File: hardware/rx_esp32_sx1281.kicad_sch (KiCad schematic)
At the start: 0 parts

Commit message: wip: schematic sheets in progress
Co-Authored-By: Claude Opus 5.5 <noreply@anthropic.com>
Claude-Session: https://claude.ai/code/session_01RFaS5jnC9tnPam9GBgmGnG
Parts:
- added AE1: ANT 2.4G wire, lib:AE_WireHole_PTH0.5mm, symbol Device:Antenna
- added AE2: 2450AT07A0100001T, lib:ANT-SMD_4P-L1.0-W0.5_Johanson_2450AT07A0100_Edge5.0x3.2, symbol lib:2450AT07A0100001T
- added C132, C133: 1.2pF, lib:C_0201_0603Metric_W, symbol Device:C
- added C73, C92: 1uF, lib:C_0201_0603Metric_W, symbol Device:C
- added C76, C83, C85, C89, C91: 100nF, lib:C_0201_0603Metric_W, symbol Device:C
- added C82: 10uF, lib:C_0402_1005Metric_W, symbol Device:C
- added C84: 1nF, lib:C_0201_0603Metric_W, symbol Device:C
- added C86, C88: 10nF, lib:C_0201_0603Metric_W, symbol Device:C
- added C87: 470nF, lib:C_0201_0603Metric_W, symbol Device:C
- added D4: RGB WS2812, lib:LED-SMD_4P-L1.0-W1.0-TL_XL-1010RGBC-WS2812B_Dense, symbol OpenDrone:XL-1010RGBC-WS2812B
- added D8: SDM02M30CLP3, lib:X2-DFN1006-3_L1.0-W0.6_SDM02M30CLP3, symbol lib:SDM02M30CLP3-7B
- added FL1: LPF 2.4G, lib:FILTER-SMD_4P-L1.0-W0.5-L_DEA102700LT-XXX_W, symbol OpenDrone:DEA102700LT-6307A2
- added R56: 10k, lib:R_0201_0603Metric_W, symbol Device:R
- added R88: 0R, lib:R_0201_0603Metric_W, symbol Device:R
- added SW1: SKUBAAE010, lib:SW_Alps_SKUBAAE010_2.4x1.4mm, symbol lib:SKUBAAE010
- added U16: ESP32-PICO-V3, lib:LGA-48_7x7mm_P0.5mm_EP_ESP32-PICO, symbol lib:ESP32-PICO-V3
- added U18: SX1281, lib:QFN-24_L4.0-W4.0-P0.50-TL-EP2.6_Dense, symbol lib:SX1281IMLTRT
- added X3: 52MHz TCXO, lib:OSC-SMD_4P-L2.0-W1.6-BL_TXC_7Z_Dense, symbol OpenDrone:OW7EL89CENUNFAYLC-52M
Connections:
- new net +3V3: C76.1, C82.1, C83.1, C85.1, C89.1, C91.1, C92.1, D4.2 (VDD), R56.1, U16.1 (VDDA), U16.19 (VDD3P3_RTC), U16.3 (VDDA3P3), U16.37 (VDD3P3_CPU), U16.4 (VDDA3P3), U16.43 (VDDA), U16.46 (VDDA), U18.11 (VBAT_IO), U18.15 (VBAT), X3.4 (VDD)
- new net BOOT_SW: D8.3 (K), SW1.1
- new net FC_BOOT: D8.1 (A1)
- new net GND: AE2.2 (GND), AE2.3 (GND), C132.2, C133.2, C73.2, C76.2, C82.2, C83.2, C85.2, C86.2, C87.1, C88.1, C89.2, C91.2, C92.2, D4.3 (GND), FL1.2 (GND), FL1.4 (GND), SW1.2, U16.49 (GND), U18.13 (GND), U18.20 (GND), U18.21 (GND), U18.23 (GND), U18.24 (GND), U18.25 (GND), U18.5 (GND), X3.1 (GND), X3.2 (GND)
- new net PA_BIAS_PWM: U16.20 (MTCK/IO13)
- new net PA_DET: U16.24 (IO4)
- new net PA_EN: U16.22 (IO2)
- new net PA_NTC: U16.10 (VDET_1/I34)
- new net RADIO_BUSY: U16.5 (SENSOR_VP/I36), U18.7 (BUSY)
- new net RADIO_DIO1: U16.6 (SENSOR_CAPP/I37), U18.8 (DIO1)
- new net RADIO_MISO: U16.13 (32K_XN/IO33), U18.16 (MISO_TX)
- new net RADIO_MOSI: U16.12 (32K_XP/IO32), U18.17 (MOSI_RX)
- new net RADIO_NSS: U16.16 (IO27), U18.19 (NSS_CTS)
- new net RADIO_RST: U16.15 (IO26), U18.3 (NRESET)
- new net RADIO_SCK: U16.14 (IO25), U18.18 (SCK_RTSN)
- new net RF_RFIO: FL1.1 (IN), U18.22 (RFIO)
- new net RF_RX_ANT: AE1.1 (A), FL1.3 (OUT)
- new net RF_WIFI: C133.1, R88.2, U16.2 (LNA_IN)
- new net RF_WIFI_ANT: AE2.1 (FEED), AE2.4 (FEED), C132.1, R88.1
- new net RX_BOOT: D8.2 (A2), U16.23 (IO0)
- new net RX_EN: C73.1, R56.2, U16.9 (EN)
- new net RX_LED: D4.4 (DIN), U16.39 (IO22)
- new net TCXO_OUT: C84.1, X3.3 (Out_Put)
- new net UART0_RX: U16.41 (U0TXD/IO1)
- new net UART0_TX: U16.40 (U0RXD/IO3)
- new net VREG_RADIO: C87.2, C88.2, U18.12 (DCC_FB), U18.2 (VDD_IN)
- new net VR_PA: C86.1, U18.1 (VR_PA)
- new net VTX_PWR_CTL: U16.42 (IO21)
- new net VTX_SPI_CLK: U16.34 (IO5)
- new net VTX_SPI_CS: U16.38 (IO19)
- new net VTX_SPI_DATA: U16.17 (MTMS/IO14)
- new net XTA: C84.2, U18.4 (XTA)
- no-connect marks 0 -> 25
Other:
- note added: "2.4 GHz LPF + wire antenna"
- note added: "Boot / bind button"
- note added: "ELRS RGB LED"
- note added: "ESP32-PICO-V3 MCU"
- note added: "SX1281 radio"
- note added: "Wi-Fi chip antenna"

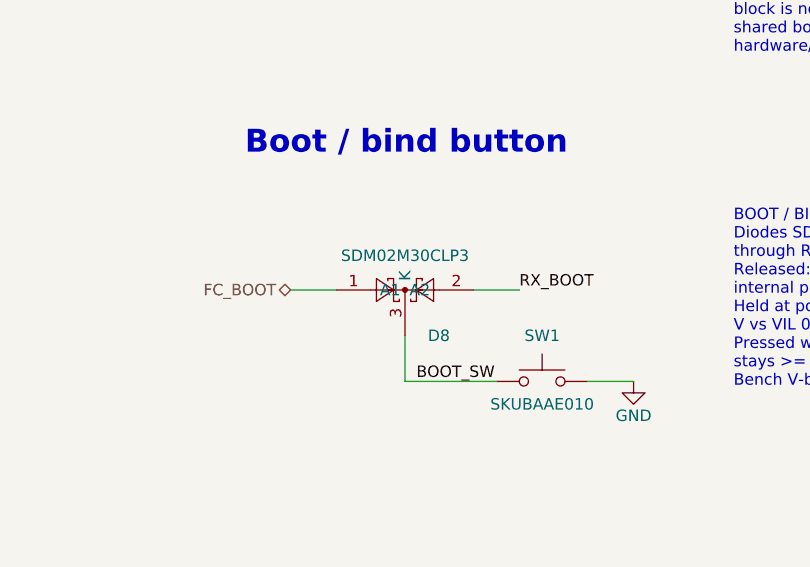
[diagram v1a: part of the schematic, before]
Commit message: wip: schematic integration in progress (saved after container restart)
Co-Authored-By: Claude Opus 5.5 <noreply@anthropic.com>
Claude-Session: https://claude.ai/code/session_01RFaS5jnC9tnPam9GBgmGnG
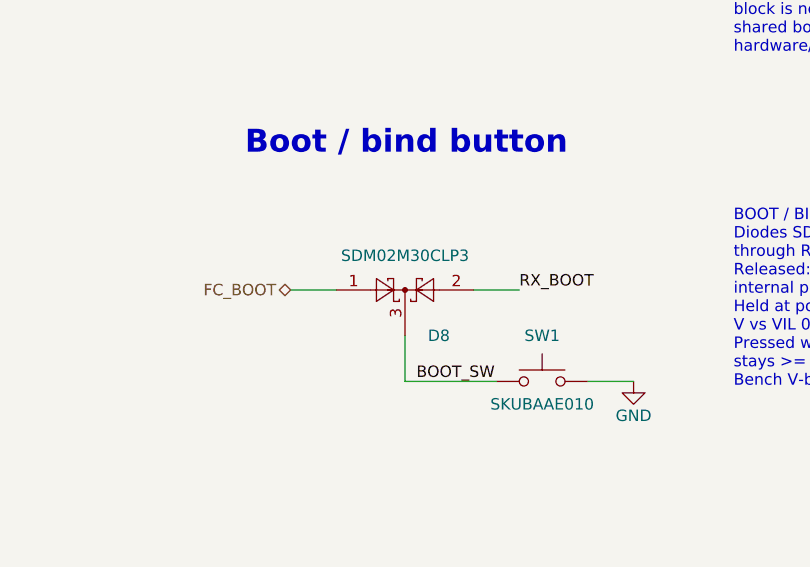
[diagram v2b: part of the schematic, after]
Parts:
- C82: LCSC (none) -> C237279
- D4: symbol OpenDrone:XL-1010RGBC-WS2812B -> lib:XL-1010RGBC-WS2812B
- FL1: symbol OpenDrone:DEA102700LT-6307A2 -> lib:DEA102700LT-6307A2
- X3: symbol OpenDrone:OW7EL89CENUNFAYLC-52M -> lib:OW7EL89CENUNFAYLC-52M
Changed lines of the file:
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@@
 		(in_pos_files no)
 		(dnp no)
-		(property "Reference" "#PWR04"
+		(property "Reference" "#PWR159"
 			(at 76.2 93.98 0)
 			(hide yes)
@@
 			(project "OpenAIO-Whoop"
 				(path "/2c3a7206-1e66-4d43-a02f-491225e20dd6/73d8a02c-e770-5e7b-9535-3e34b447ded8"
-					(reference "#PWR04")
+					(reference "#PWR159")
 					(unit 1)
 				)
@@
 		(in_pos_files no)
 		(dnp no)
-		(property "Reference" "#PWR02"
+		(property "Reference" "#PWR155"
 			(at 109.22 66.04 0)
 			(hide yes)
@@
 			(project "OpenAIO-Whoop"
 				(path "/2c3a7206-1e66-4d43-a02f-491225e20dd6/73d8a02c-e770-5e7b-9535-3e34b447ded8"
-					(reference "#PWR02")
+					(reference "#PWR155")
 					(unit 1)
 				)
@@
 		(in_pos_files no)
 		(dnp no)
-		(property "Reference" "#PWR07"
+		(property "Reference" "#PWR165"
 			(at 125.73 139.7 0)
 			(hide yes)
@@
 			(project "OpenAIO-Whoop"
 				(path "/2c3a7206-1e66-4d43-a02f-491225e20dd6/73d8a02c-e770-5e7b-9535-3e34b447ded8"
-					(reference "#PWR07")
+					(reference "#PWR165")
 					(unit 1)
 				)
@@
 		(in_pos_files no)
 		(dnp no)
-		(property "Reference" "#PWR15"
+		(property "Reference" "#PWR168"
 			(at 292.1 171.45 0)
 			(hide yes)
@@
 			(project "OpenAIO-Whoop"
 				(path "/2c3a7206-1e66-4d43-a02f-491225e20dd6/73d8a02c-e770-5e7b-9535-3e34b447ded8"
-					(reference "#PWR15")
+					(reference "#PWR168")
 					(unit 1)
 				)
@@
 		(in_pos_files no)
 		(dnp no)
-		(property "Reference" "#PWR21"
+		(property "Reference" "#PWR176"
 			(at 182.88 207.01 0)
 			(hide yes)
@@
 			(project "OpenAIO-Whoop"
 				(path "/2c3a7206-1e66-4d43-a02f-491225e20dd6/73d8a02c-e770-5e7b-9535-3e34b447ded8"
-					(reference "#PWR21")
+					(reference "#PWR176")
 					(unit 1)
 				)
@@
 			)
 		)
-		(property "LCSC" ""
+		(property "LCSC" "C237279"
 			(at 292.1 171.45 0)
 			(hide yes)
@@
 	)
 	(symbol
-		(lib_id "OpenDrone:OW7EL89CENUNFAYLC-52M")
+		(lib_id "lib:OW7EL89CENUNFAYLC-52M")
 		(at 71.12 118.11 0)
 		(unit 1)
@@
 	)
 	(symbol
-		(lib_id "OpenDrone:DEA102700LT-6307A2")
+		(lib_id "lib:DEA102700LT-6307A2")
 		(at 166.37 116.84 0)
 		(unit 1)
@@
 		(in_pos_files no)
 		(dnp no)
-		(property "Reference" "#PWR11"
+		(property "Reference" "#PWR164"
 			(at 166.37 130.81 0)
 			(hide yes)
@@
 			(project "OpenAIO-Whoop"
 				(path "/2c3a7206-1e66-4d43-a02f-491225e20dd6/73d8a02c-e770-5e7b-9535-3e34b447ded8"
-					(reference "#PWR11")
+					(reference "#PWR164")
 					(unit 1)
 				)
@@
 		(in_pos_files no)
 		(dnp no)
-		(property "Reference" "#PWR10"
+		(property "Reference" "#PWR161"
 			(at 157.48 115.57 0)
 			(hide yes)
@@
 			(project "OpenAIO-Whoop"
 				(path "/2c3a7206-1e66-4d43-a02f-491225e20dd6/73d8a02c-e770-5e7b-9535-3e34b447ded8"
-					(reference "#PWR10")
+					(reference "#PWR161")
 					(unit 1)
 				)
@@
 		(in_pos_files no)
 		(dnp no)
-		(property "Reference" "#PWR17"
+		(property "Reference" "#PWR169"
 			(at 213.36 173.99 0)
 			(hide yes)
@@
 			(project "OpenAIO-Whoop"
 				(path "/2c3a7206-1e66-4d43-a02f-491225e20dd6/73d8a02c-e770-5e7b-9535-3e34b447ded8"
-					(reference "#PWR17")
+					(reference "#PWR169")
 					(unit 1)
 				)
@@
 		(in_pos_files no)
 		(dnp no)
-		(property "Reference" "#PWR16"
+		(property "Reference" "#PWR171"
 			(at 292.1 181.61 0)
 			(hide yes)
@@
 			(project "OpenAIO-Whoop"
 				(path "/2c3a7206-1e66-4d43-a02f-491225e20dd6/73d8a02c-e770-5e7b-9535-3e34b447ded8"
-					(reference "#PWR16")
+					(reference "#PWR171")
 					(unit 1)
 				)
@@
 		(in_pos_files no)
 		(dnp no)
-		(property "Reference" "#PWR14"
+		(property "Reference" "#PWR170"
 			(at 279.4 181.61 0)
 			(hide yes)
@@
 			(project "OpenAIO-Whoop"
 				(path "/2c3a7206-1e66-4d43-a02f-491225e20dd6/73d8a02c-e770-5e7b-9535-3e34b447ded8"
-					(reference "#PWR14")
+					(reference "#PWR170")
 					(unit 1)
 				)
@@
 		(in_pos_files no)
 		(dnp no)
-		(property "Reference" "#PWR06"
+		(property "Reference" "#PWR160"
 			(at 83.82 107.95 0)
 			(hide yes)
@@
 			(project "OpenAIO-Whoop"
 				(path "/2c3a7206-1e66-4d43-a02f-491225e20dd6/73d8a02c-e770-5e7b-9535-3e34b447ded8"
-					(reference "#PWR06")
+					(reference "#PWR160")
 					(unit 1)
 				)
@@
 		(in_pos_files no)
 		(dnp no)
-		(property "Reference" "#PWR09"
+		(property "Reference" "#PWR163"
 			(at 104.14 128.27 0)
 			(hide yes)
@@
 			(project "OpenAIO-Whoop"
 				(path "/2c3a7206-1e66-4d43-a02f-491225e20dd6/73d8a02c-e770-5e7b-9535-3e34b447ded8"
-					(reference "#PWR09")
+					(reference "#PWR163")
 					(unit 1)
 				)
@@
 		(in_pos_files no)
 		(dnp no)
-		(property "Reference" "#PWR26"
+		(property "Reference" "#PWR178"
 			(at 71.12 210.82 0)
 			(hide yes)
@@
 			(project "OpenAIO-Whoop"
 				(path "/2c3a7206-1e66-4d43-a02f-491225e20dd6/73d8a02c-e770-5e7b-9535-3e34b447ded8"
-					(reference "#PWR26")
+					(reference "#PWR178")
 					(unit 1)
 				)
@@
 		(in_pos_files no)
 		(dnp no)
-		(property "Reference" "#PWR18"
+		(property "Reference" "#PWR172"
 			(at 205.74 191.77 0)
 			(hide yes)
@@
 			(project "OpenAIO-Whoop"
 				(path "/2c3a7206-1e66-4d43-a02f-491225e20dd6/73d8a02c-e770-5e7b-9535-3e34b447ded8"
-					(reference "#PWR18")
+					(reference "#PWR172")
 					(unit 1)
 				)
@@
 		(in_pos_files no)
 		(dnp no)
-		(property "Reference" "#PWR13"
+		(property "Reference" "#PWR167"
 			(at 279.4 171.45 0)
 			(hide yes)
@@
 			(project "OpenAIO-Whoop"
 				(path "/2c3a7206-1e66-4d43-a02f-491225e20dd6/73d8a02c-e770-5e7b-9535-3e34b447ded8"
-					(reference "#PWR13")
+					(reference "#PWR167")
 					(unit 1)
 				)
@@
 		(in_pos_files no)
 		(dnp no)
-		(property "Reference" "#PWR12"
+		(property "Reference" "#PWR166"
 			(at 228.6 171.45 0)
 			(hide yes)
@@
 			(project "OpenAIO-Whoop"
 				(path "/2c3a7206-1e66-4d43-a02f-491225e20dd6/73d8a02c-e770-5e7b-9535-3e34b447ded8"
-					(reference "#PWR12")
+					(reference "#PWR166")
 					(unit 1)
 				)
@@
 		(in_pos_files no)
 		(dnp no)
-		(property "Reference" "#PWR19"
+		(property "Reference" "#PWR180"
 			(at 233.68 252.73 0)
 			(hide yes)
@@
 			(project "OpenAIO-Whoop"
 				(path "/2c3a7206-1e66-4d43-a02f-491225e20dd6/73d8a02c-e770-5e7b-9535-3e34b447ded8"
-					(reference "#PWR19")
+					(reference "#PWR180")
 					(unit 1)
 				)
@@
 		(in_pos_files no)
 		(dnp no)
-		(property "Reference" "#PWR03"
+		(property "Reference" "#PWR156"
 			(at 77.47 77.47 0)
 			(hide yes)
@@
 			(project "OpenAIO-Whoop"
 				(path "/2c3a7206-1e66-4d43-a02f-491225e20dd6/73d8a02c-e770-5e7b-9535-3e34b447ded8"
-					(reference "#PWR03")
+					(reference "#PWR156")
 					(unit 1)
 				)
@@
 		(in_pos_files no)
 		(dnp no)
-		(property "Reference" "#PWR23"
+		(property "Reference" "#PWR173"
 			(at 93.98 195.58 0)
 			(hide yes)
@@
 			(project "OpenAIO-Whoop"
 				(path "/2c3a7206-1e66-4d43-a02f-491225e20dd6/73d8a02c-e770-5e7b-9535-3e34b447ded8"
-					(reference "#PWR23")
+					(reference "#PWR173")
 					(unit 1)
 				)
@@
 		(in_pos_files no)
 		(dnp no)
-		(property "Reference" "#PWR25"
+		(property "Reference" "#PWR179"
 			(at 102.87 215.9 0)
 			(hide yes)
@@
 			(project "OpenAIO-Whoop"
 				(path "/2c3a7206-1e66-4d43-a02f-491225e20dd6/73d8a02c-e770-5e7b-9535-3e34b447ded8"
-					(reference "#PWR25")
+					(reference "#PWR179")
 					(unit 1)
 				)
@@
 		(in_pos_files no)
 		(dnp no)
-		(property "Reference" "#PWR24"
+		(property "Reference" "#PWR174"
 			(at 71.12 200.66 0)
 			(hide yes)
@@
 			(project "OpenAIO-Whoop"
 				(path "/2c3a7206-1e66-4d43-a02f-491225e20dd6/73d8a02c-e770-5e7b-9535-3e34b447ded8"
-					(reference "#PWR24")
+					(reference "#PWR174")
 					(unit 1)
 				)
@@
 		(in_pos_files no)
 		(dnp no)
-		(property "Reference" "#PWR27"
+		(property "Reference" "#PWR158"
 			(at 289.56 85.09 0)
 			(hide yes)
@@
 			(project "OpenAIO-Whoop"
 				(path "/2c3a7206-1e66-4d43-a02f-491225e20dd6/73d8a02c-e770-5e7b-9535-3e34b447ded8"
-					(reference "#PWR27")
+					(reference "#PWR158")
 					(unit 1)
 				)
@@
 		(in_pos_files no)
 		(dnp no)
-		(property "Reference" "#PWR20"
+		(property "Reference" "#PWR177"
 			(at 203.2 207.01 0)
 			(hide yes)
@@
 			(project "OpenAIO-Whoop"
 				(path "/2c3a7206-1e66-4d43-a02f-491225e20dd6/73d8a02c-e770-5e7b-9535-3e34b447ded8"
-					(reference "#PWR20")
+					(reference "#PWR177")
 					(unit 1)
 				)
@@
 	)
 	(symbol
-		(lib_id "OpenDrone:XL-1010RGBC-WS2812B")
+		(lib_id "lib:XL-1010RGBC-WS2812B")
 		(at 97.79 200.66 0)
 		(unit 1)
@@
 		(in_pos_files no)
 		(dnp no)
-		(property "Reference" "#PWR05"
+		(property "Reference" "#PWR157"
 			(at 163.83 85.09 0)
 			(hide yes)
@@
 			(project "OpenAIO-Whoop"
 				(path "/2c3a7206-1e66-4d43-a02f-491225e20dd6/73d8a02c-e770-5e7b-9535-3e34b447ded8"
-					(reference "#PWR05")
+					(reference "#PWR157")
 					(unit 1)
 				)
@@
 		(in_pos_files no)
 		(dnp no)
-		(property "Reference" "#PWR22"
+		(property "Reference" "#PWR175"
 			(at 165.1 204.47 0)
 			(hide yes)
@@
 			(project "OpenAIO-Whoop"
 				(path "/2c3a7206-1e66-4d43-a02f-491225e20dd6/73d8a02c-e770-5e7b-9535-3e34b447ded8"
-					(reference "#PWR22")
+					(reference "#PWR175")
 					(unit 1)
 				)
@@
 		(in_pos_files no)
 		(dnp no)
-		(property "Reference" "#PWR01"
+		(property "Reference" "#PWR154"
 			(at 109.22 55.88 0)
 			(hide yes)
@@
 			(project "OpenAIO-Whoop"
 				(path "/2c3a7206-1e66-4d43-a02f-491225e20dd6/73d8a02c-e770-5e7b-9535-3e34b447ded8"
-					(reference "#PWR01")
+					(reference "#PWR154")
 					(unit 1)
 				)
@@
 		(in_pos_files no)
 		(dnp no)
-		(property "Reference" "#PWR08"
+		(property "Reference" "#PWR162"
 			(at 54.61 128.27 0)
 			(hide yes)
@@
 			(project "OpenAIO-Whoop"
 				(path "/2c3a7206-1e66-4d43-a02f-491225e20dd6/73d8a02c-e770-5e7b-9535-3e34b447ded8"
-					(reference "#PWR08")
+					(reference "#PWR162")
 					(unit 1)
 				)

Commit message: schematic: integrated (ERC 0 errors / 2 justified warnings; check_netlist 7/7; conventions 0 FAIL; visual 0 hits; 268/268 refs match bom_plan; FC+RX pin maps match PINMAP)
Co-Authored-By: Claude Opus 5.5 <noreply@anthropic.com>
Claude-Session: https://claude.ai/code/session_01RFaS5jnC9tnPam9GBgmGnG
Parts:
- FL1: value LPF 2.4G -> 2450FM07D0034T; footprint lib:FILTER-SMD_4P-L1.0-W0.5-L_DEA102700LT-XXX_W -> lib:FILTER-SMD_4P-L1.0-W0.5-L_W; symbol lib:DEA102700LT-6307A2 -> lib:2450FM07D0034T; LCSC C574024 -> C2651081; MPN DEA102700LT-6307A2 -> 2450FM07D0034T; Manufacturer TDK -> Johanson Technology
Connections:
- net PA_BIAS_PWM renamed VTX_AMP_PWM
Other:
- note added: "BOOT / BIND BUTTON (D65)"
- note added: "ESP32-PICO-V3 MCU (ELRS)"
- note added: "NOTES"
- note added: "SX1281 RADIO + 2.4 GHz FILTER + WIRE ANTENNA"
- note added: "Wi-Fi CHIP ANTENNA (D58)"
- note removed: "2.4 GHz LPF + wire antenna"
- note removed: "Boot / bind button"
- note removed: "ESP32-PICO-V3 MCU"
- note removed: "SX1281 radio"
- note removed: "Wi-Fi chip antenna"
- moved on the sheet: AE2, C132, C133, C73, FL1, R88

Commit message: hardware: floorplan v3 review pass (RX RF corner blocker fixed; majors listed in FLOORPLAN.md Open)
Co-Authored-By: Claude Opus 5.5 <noreply@anthropic.com>
Claude-Session: https://claude.ai/code/session_01RFaS5jnC9tnPam9GBgmGnG
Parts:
- AE1: value ANT 2.4G wire -> ANT
